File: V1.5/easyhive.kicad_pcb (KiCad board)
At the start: 2 copper layers, 35 x 75 mm, 104 parts, among them IC1 ATSAMD21G, IC2 BQ2407X, IC3 ADS1232, IC4 DS18B20U, IC5 XC6220B331, IC6 SARA-N310, IC7 TPS22919, J1 U.FL, J2 U.FL(2), K1 693043020611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

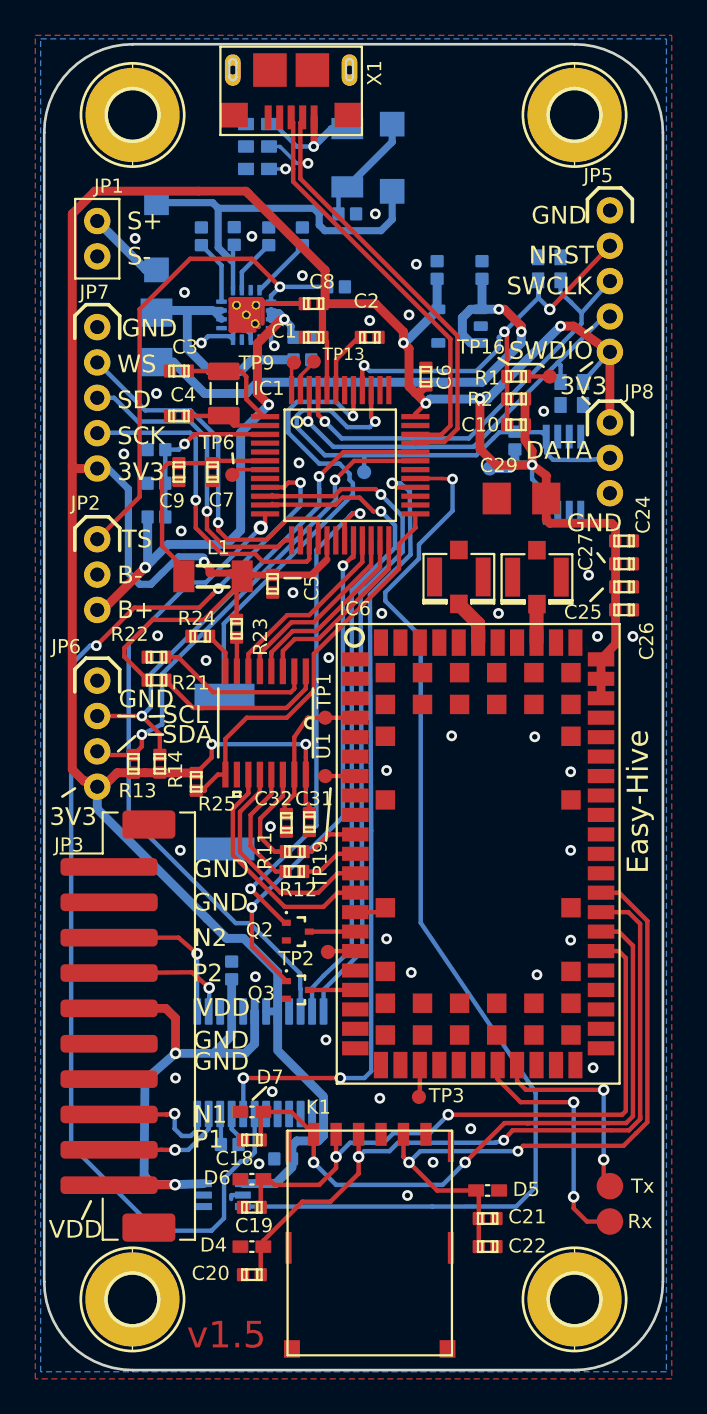
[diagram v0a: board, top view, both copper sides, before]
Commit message: Hardware optimization after Prototyp
- PA12: TX 3V3
- PA13: RX 3V3
- PA14: RTS 3V3
- PA15: CTS 3V3
- insert 2x R0 between TX/RX track
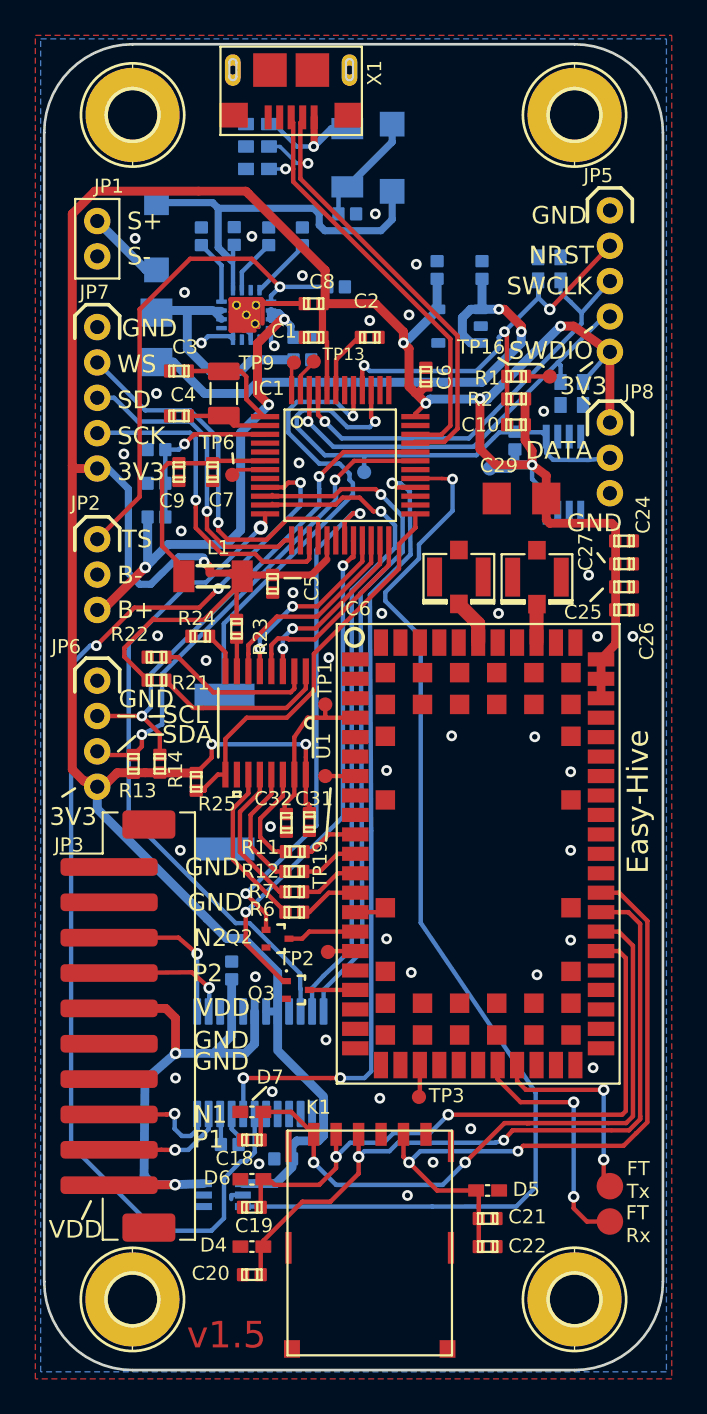
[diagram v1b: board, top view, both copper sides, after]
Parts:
- added R6: 0R, easyhive:C0402, F.Cu at (145.2, 116.6)
- added R7: 0R, easyhive:C0402, F.Cu at (145.2, 115.5)
- D1, D2: footprint easyhive:SOD-123 -> easyhive:SOD123
- L1, L2: value (none) -> SM-1206
- moved Q2 1.22 mm to (144.2, 118.1)
- moved TP1 0.75 mm to (146.9, 104.8)
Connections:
- IC1 pad 14: /I2S_MCK -> (no net)
- IC1 pad 21: /SARA_RX_3V3 -> /SARA_TX_3V3
- IC1 pad 22: /SARA_TX_3V3 -> /SARA_RX_3V3
- IC1 pad 23: /SARA_CTS_3V3 -> /SARA_RTS_3V3
- IC1 pad 24: /SARA_RTS_3V3 -> /SARA_CTS_3V3
- IC1 pad 26: /RED -> (no net)
- IC1 pad 27: /GREEN -> (no net)
- IC1 pad 30: /BLUE -> (no net)
- IC1 pad 37: Net-(IC1-Pad37) -> (no net)
- IC1 pad 38: Net-(IC1-Pad38) -> (no net)
- IC1 pad 4: Net-(IC1-Pad4) -> (no net)
- IC1 pad 8: Net-(IC1-Pad8) -> (no net)
- IC2 pad 7: Net-(IC2-Pad7) -> (no net)
- IC2 pad 9: Net-(IC2-Pad9) -> (no net)
- IC3 pad 4: Net-(IC3-Pad4) -> (no net)
- IC6 pad 12: /SARA_TX_1V8 -> Net-(IC6-Pad12)
- IC6 pad 13: /SARA_RX_1V8 -> Net-(IC6-Pad13)
- IC6 pad 26: /SARA_SDA -> (no net)
- IC6 pad 27: /SARA_SCL -> (no net)
- IC6 pad 62: /ANT_DET -> (no net)
- IC7 pad 5: Net-(IC7-Pad5) -> (no net)
- K1 pad C6: Net-(K1-PadC6) -> (no net)
- X1 pad 4: Net-(X1-Pad4) -> (no net)
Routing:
- net /SARA_TX_1V8: track 12.8 -> 8.36 mm
- net /SARA_RX_1V8: track 13.4 -> 9.38 mm
- net Net-(IC6-Pad13): track 0.00 -> 3.41 mm
- net Net-(IC6-Pad12): track 0.00 -> 3.38 mm
- net Net-(IC6-Pad15): track 2.61 -> 3.92 mm
- net GND: track 18.9 -> 17.9 mm
- net /SARA_RX_3V3: track 10.8 -> 11.6 mm
- net /+1V8: track 8.65 -> 9.43 mm
- net /SARA_CTS_3V3: track 10.8 -> 11.4 mm
- net /SARA_RTS_3V3: track 10.7 -> 10.2 mm, vias 0 -> 2
- net /SARA_TX_3V3: track 10.8 -> 10.3 mm, vias 0 -> 2
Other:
- board text added: "FT Rx"
- board text added: "FT Tx"
- board text removed: "Rx"
- board text removed: "Tx"
